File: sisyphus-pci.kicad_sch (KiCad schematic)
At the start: 124 parts, among them J1 Bus_PCI_32bit_Universal, J10 LINE_OUT, J2 JOYSTICK, J3 CD_IN, J4 WAVE_BLASTER, J5 LINE_IN_HDR, J6 LINE_IN_3.5, J7 HEADPHONE_OUT, J8 PCPCI, J9 LINE_OUT_3.5M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

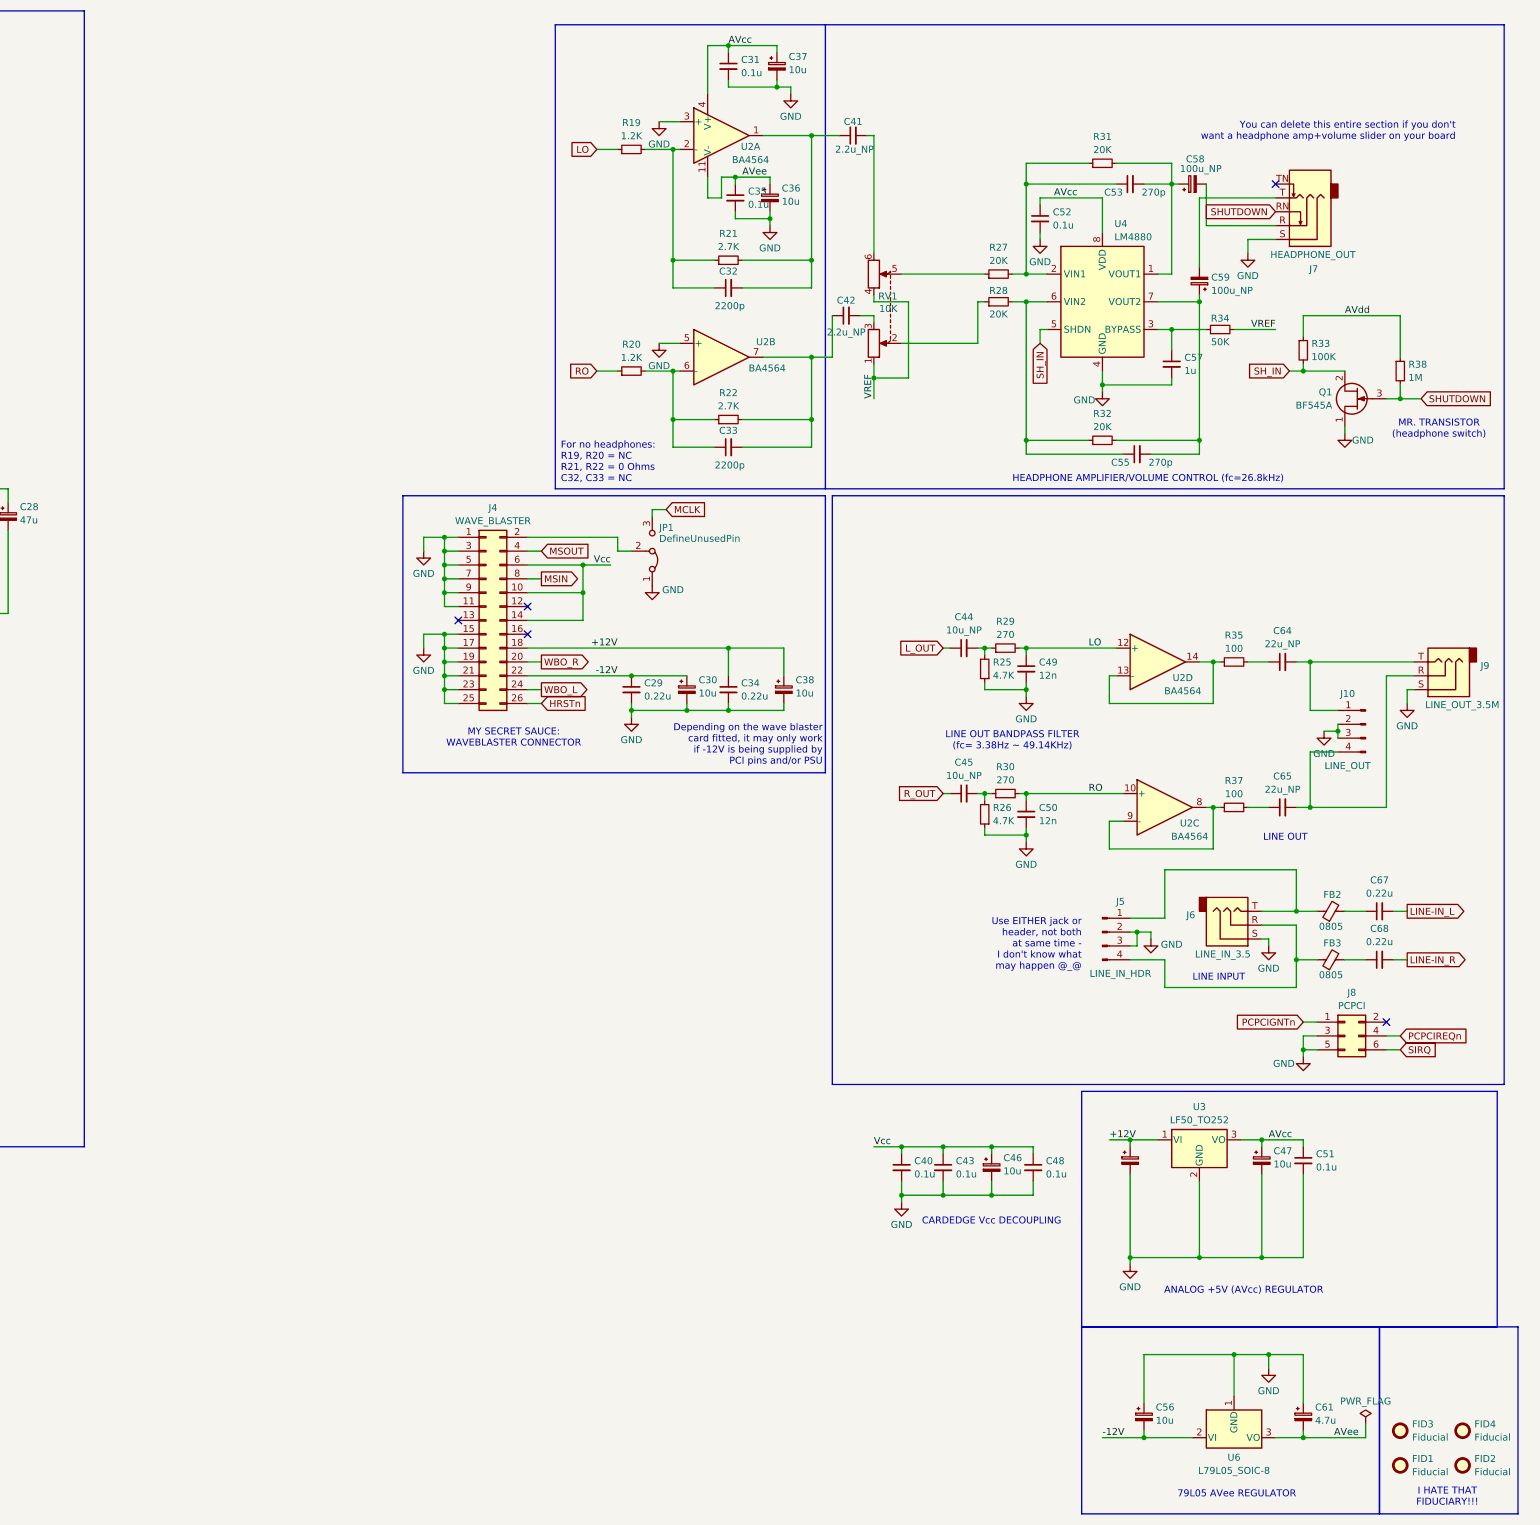
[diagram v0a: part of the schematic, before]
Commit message: Add files via upload
MAJOR fixes to spacing and what not. Also made a CSV BOM.
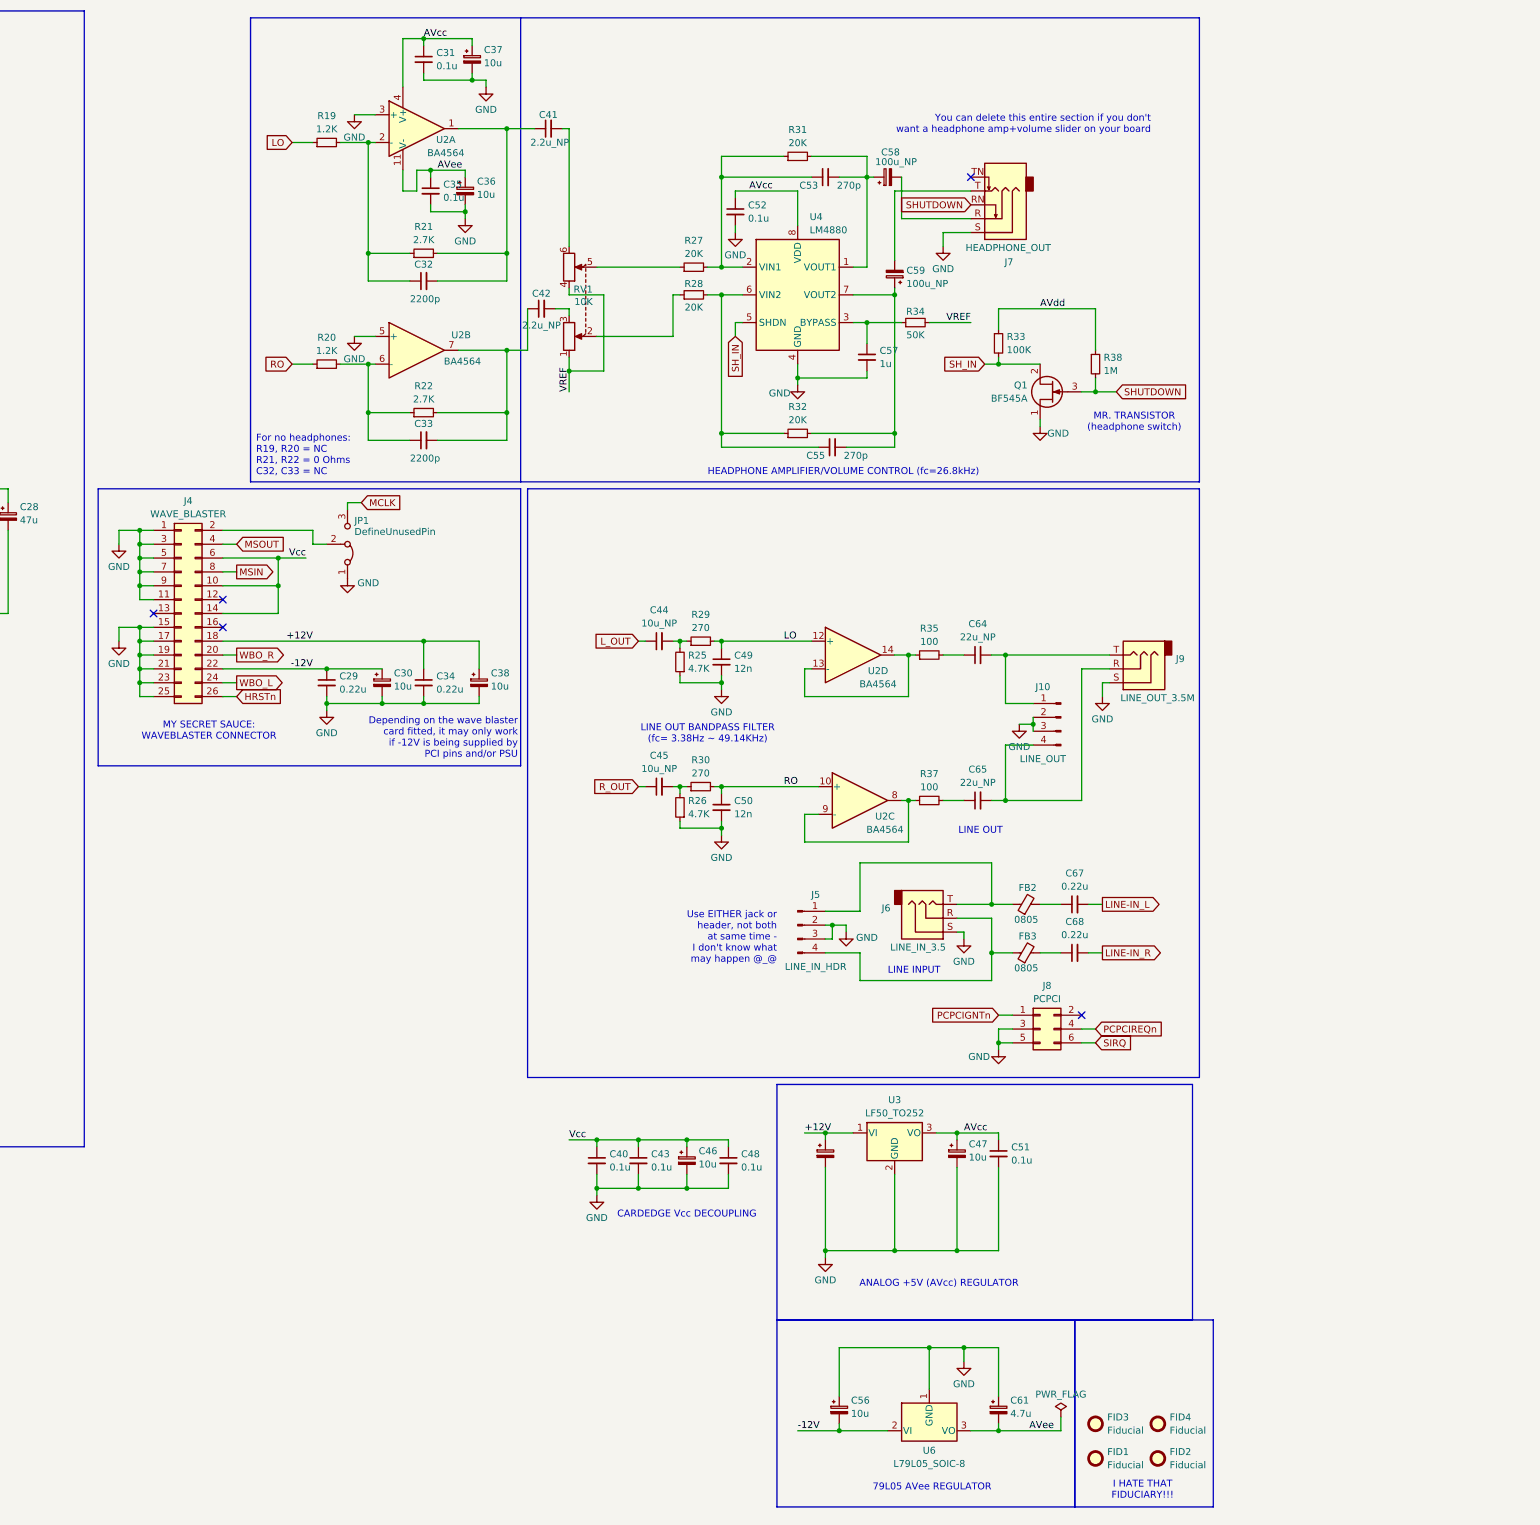
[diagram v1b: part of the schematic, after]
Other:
- moved on the sheet: C29, C30, C31, C32, C33, C34, C35, C36, C37, C38, C40, C41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

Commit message: Add files via upload
Updated to version 0.1a
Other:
- moved on the sheet: C32, C35, C36, R21
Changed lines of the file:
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@@
 	)
 	(junction
-		(at 396.24 57.15)
+		(at 396.24 58.42)
 		(diameter 0)
 		(color 0 0 0 0)
@@
 	)
 	(junction
-		(at 388.62 49.53)
+		(at 388.62 52.07)
 		(diameter 0)
 		(color 0 0 0 0)
@@
 	)
 	(junction
-		(at 382.27 41.91)
+		(at 382.27 44.45)
 		(diameter 0)
 		(color 0 0 0 0)
@@
 	)
 	(junction
-		(at 370.84 57.15)
+		(at 370.84 58.42)
 		(diameter 0)
 		(color 0 0 0 0)
@@
 	(wire
 		(pts
-			(xy 382.27 48.26) (xy 382.27 49.53)
+			(xy 382.27 50.8) (xy 382.27 52.07)
 		)
 		(stroke
@@
 	(wire
 		(pts
-			(xy 396.24 34.29) (xy 396.24 57.15)
+			(xy 396.24 34.29) (xy 396.24 58.42)
 		)
 		(stroke
@@
 	(wire
 		(pts
-			(xy 377.19 45.72) (xy 379.73 45.72)
+			(xy 377.19 44.45) (xy 382.27 44.45)
 		)
 		(stroke
@@
 	(wire
 		(pts
-			(xy 370.84 62.23) (xy 378.46 62.23)
+			(xy 370.84 63.5) (xy 378.46 63.5)
 		)
 		(stroke
@@
 	(wire
 		(pts
-			(xy 388.62 41.91) (xy 388.62 43.18)
+			(xy 388.62 44.45) (xy 388.62 45.72)
 		)
 		(stroke
@@
 	(wire
 		(pts
-			(xy 382.27 41.91) (xy 388.62 41.91)
+			(xy 382.27 44.45) (xy 388.62 44.45)
 		)
 		(stroke
@@
 	(wire
 		(pts
-			(xy 379.73 45.72) (xy 379.73 41.91)
-		)
-		(stroke
-			(width 0)
-			(type default)
-		)
-	)
-	(wire
-		(pts
 			(xy 90.17 34.29) (xy 101.6 34.29)
 		)
@@
 	(wire
 		(pts
-			(xy 377.19 41.91) (xy 377.19 45.72)
+			(xy 377.19 41.91) (xy 377.19 44.45)
 		)
 		(stroke
@@
 	(wire
 		(pts
-			(xy 379.73 41.91) (xy 382.27 41.91)
-		)
-		(stroke
-			(width 0)
-			(type default)
-		)
-	)
-	(wire
-		(pts
 			(xy 252.73 163.83) (xy 259.08 163.83)
 		)
@@
 	(wire
 		(pts
-			(xy 370.84 57.15) (xy 378.46 57.15)
+			(xy 370.84 58.42) (xy 378.46 58.42)
 		)
 		(stroke
@@
 	(wire
 		(pts
-			(xy 388.62 49.53) (xy 388.62 50.8)
+			(xy 388.62 52.07) (xy 388.62 53.34)
 		)
 		(stroke
@@
 	(wire
 		(pts
-			(xy 382.27 49.53) (xy 388.62 49.53)
+			(xy 382.27 52.07) (xy 388.62 52.07)
 		)
 		(stroke
@@
 	(wire
 		(pts
-			(xy 382.27 41.91) (xy 382.27 43.18)
+			(xy 382.27 44.45) (xy 382.27 45.72)
 		)
 		(stroke
@@
 	(wire
 		(pts
-			(xy 396.24 62.23) (xy 396.24 57.15)
+			(xy 396.24 63.5) (xy 396.24 58.42)
 		)
 		(stroke
@@
 	(wire
 		(pts
-			(xy 383.54 62.23) (xy 396.24 62.23)
+			(xy 383.54 63.5) (xy 396.24 63.5)
 		)
 		(stroke
@@
 	(wire
 		(pts
-			(xy 396.24 57.15) (xy 383.54 57.15)
+			(xy 396.24 58.42) (xy 383.54 58.42)
 		)
 		(stroke
@@
 	(wire
 		(pts
-			(xy 370.84 57.15) (xy 370.84 62.23)
+			(xy 370.84 58.42) (xy 370.84 63.5)
 		)
 		(stroke
@@
 	(wire
 		(pts
-			(xy 370.84 36.83) (xy 370.84 57.15)
+			(xy 370.84 36.83) (xy 370.84 58.42)
 		)
 		(stroke
@@
 	(wire
 		(pts
-			(xy 388.62 48.26) (xy 388.62 49.53)
+			(xy 388.62 50.8) (xy 388.62 52.07)
 		)
 		(stroke
@@
 	)
 	(label "AVee"
-		(at 383.54 41.91 0)
+		(at 383.54 44.45 0)
 		(fields_autoplaced yes)
 		(effects
@@
 	(symbol
 		(lib_id "Device:C_Small")
-		(at 382.27 45.72 0)
+		(at 382.27 48.26 0)
 		(unit 1)
 		(exclude_from_sim no)
@@
 		(on_board yes)
 		(dnp no)
-		(fields_autoplaced yes)
 		(property "Reference" "C35"
-			(at 384.5941 44.5141 0)
+			(at 376.174 46.99 0)
 			(effects
 				(font
@@
 		)
 		(property "Value" "0.1u"
-			(at 384.5941 46.9384 0)
+			(at 376.174 49.4143 0)
 			(effects
 				(font
@@
 		)
 		(property "Footprint" "Capacitor_SMD:C_0805_2012Metric"
-			(at 382.27 45.72 0)
+			(at 382.27 48.26 0)
 			(effects
 				(font
@@
 		)
 		(property "Datasheet" "~"
-			(at 382.27 45.72 0)
+			(at 382.27 48.26 0)
 			(effects
 				(font
@@
 		)
 		(property "Description" "Unpolarized capacitor, small symbol"
-			(at 382.27 45.72 0)
+			(at 382.27 48.26 0)
 			(effects
 				(font
@@
 	(symbol
 		(lib_id "Device:C_Polarized_Small")
-		(at 388.62 45.72 0)
+		(at 388.62 48.26 0)
 		(unit 1)
 		(exclude_from_sim no)
@@
 		(fields_autoplaced yes)
 		(property "Reference" "C36"
-			(at 390.779 43.9617 0)
+			(at 390.779 46.5017 0)
 			(effects
 				(font
@@
 		)
 		(property "Value" "10u"
-			(at 390.779 46.386 0)
+			(at 390.779 48.926 0)
 			(effects
 				(font
@@
 		)
 		(property "Footprint" "Capacitor_SMD:C_1206_3216Metric"
-			(at 388.62 45.72 0)
+			(at 388.62 48.26 0)
 			(effects
 				(font
@@
 		)
 		(property "Datasheet" "~"
-			(at 388.62 45.72 0)
+			(at 388.62 48.26 0)
 			(effects
 				(font
@@
 		)
 		(property "Description" "Polarized capacitor, small symbol"
-			(at 388.62 45.72 0)
+			(at 388.62 48.26 0)
 			(effects
 				(font
@@
 	(symbol
 		(lib_id "Device:R_Small")
-		(at 381 57.15 90)
+		(at 381 58.42 90)
 		(unit 1)
 		(exclude_from_sim no)
@@
 		(on_board yes)
 		(dnp no)
-		(fields_autoplaced yes)
 		(property "Reference" "R21"
-			(at 381 52.2689 90)
+			(at 381 56.0789 90)
 			(effects
 				(font
@@
 		)
 		(property "Value" "2.7K"
-			(at 381 54.6932 90)
+			(at 385.064 57.404 90)
 			(effects
 				(font
@@
 		)
 		(property "Footprint" "Resistor_SMD:R_0805_2012Metric"
-			(at 381 57.15 0)
+			(at 381 58.42 0)
 			(effects
 				(font
@@
 		)
 		(property "Datasheet" "~"
-			(at 381 57.15 0)
+			(at 381 58.42 0)
 			(effects
 				(font
@@
 		)
 		(property "Description" "Resistor, small symbol"
-			(at 381 57.15 0)
+			(at 381 58.42 0)
 			(effects
 				(font
@@
 	(symbol
 		(lib_id "power:GND")
-		(at 388.62 50.8 0)
+		(at 388.62 53.34 0)
 		(unit 1)
 		(exclude_from_sim no)
@@
 		(on_board yes)
 		(dnp no)
-		(fields_autoplaced yes)
 		(property "Reference" "#PWR016"
-			(at 388.62 57.15 0)
+			(at 388.62 59.69 0)
 			(effects
 				(font
@@
 		)
 		(property "Value" "GND"
-			(at 388.62 54.9331 0)
+			(at 392.176 54.61 0)
 			(effects
 				(font
@@
 		)
 		(property "Footprint" ""
-			(at 388.62 50.8 0)
+			(at 388.62 53.34 0)
 			(effects
 				(font
@@
 		)
 		(property "Datasheet" ""
-			(at 388.62 50.8 0)
+			(at 388.62 53.34 0)
 			(effects
 				(font
@@
 		)
 		(property "Description" "Power symbol creates a global label with name \"GND\" , ground"
-			(at 388.62 50.8 0)
+			(at 388.62 53.34 0)
 			(effects
 				(font
@@
 	(symbol
 		(lib_id "Device:C_Small")
-		(at 381 62.23 90)
+		(at 381 63.5 90)
 		(unit 1)
 		(exclude_from_sim no)
@@
 		(dnp no)
 		(property "Reference" "C32"
-			(at 381 59.182 90)
+			(at 381 60.452 90)
 			(effects
 				(font
@@
 		)
 		(property "Value" "2200p"
-			(at 381.254 65.532 90)
+			(at 385.826 62.23 90)
 			(effects
 				(font
@@
 		)
 		(property "Footprint" "Capacitor_SMD:C_0805_2012Metric"
-			(at 381 62.23 0)
+			(at 381 63.5 0)
 			(effects
 				(font
@@
 		)
 		(property "Datasheet" "~"
-			(at 381 62.23 0)
+			(at 381 63.5 0)
 			(effects
 				(font
@@
 		)
 		(property "Description" "Unpolarized capacitor, small symbol"
-			(at 381 62.23 0)
+			(at 381 63.5 0)
 			(effects
 				(font
